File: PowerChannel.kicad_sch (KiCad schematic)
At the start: 15 parts, among them J1 Screw_Terminal_01x04, Q1 2N7002, Q2 NTF6P02, Q3 2N7002, U12 INA219xID

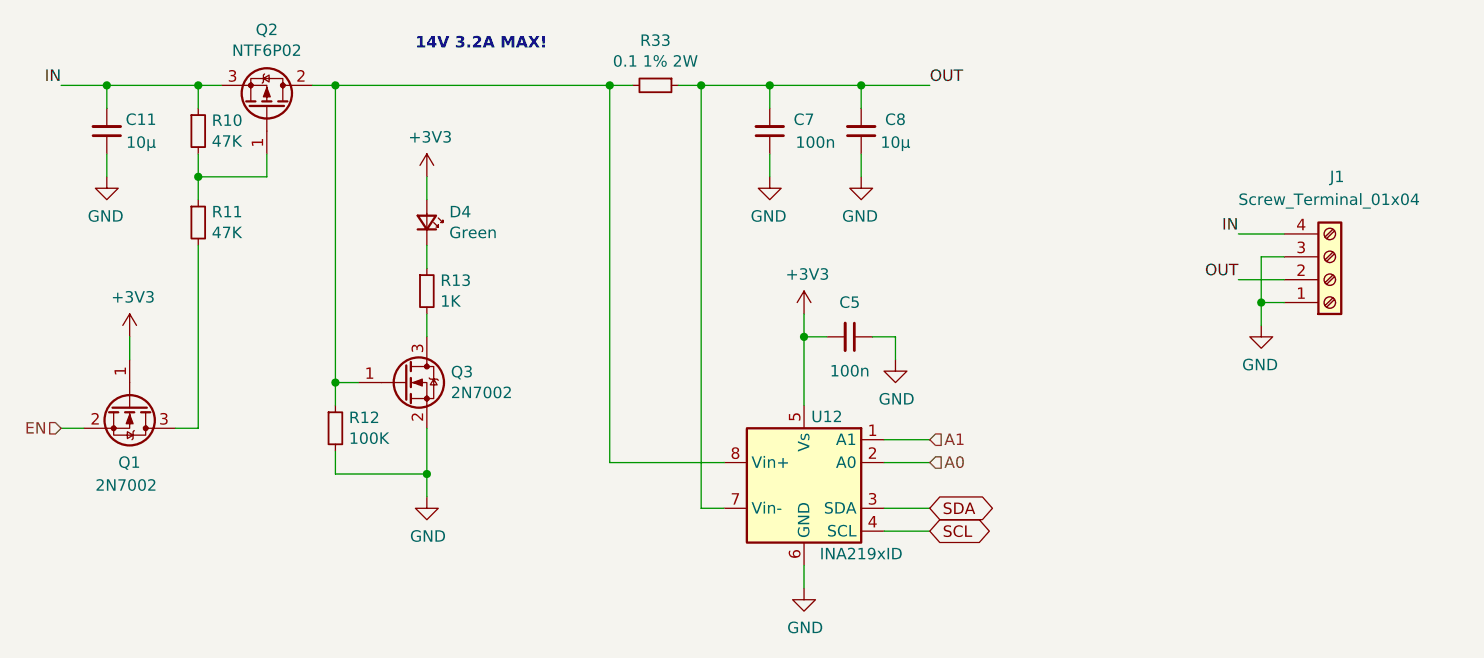
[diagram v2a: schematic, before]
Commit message: Schematic: Replace Teensy 3.2 by PCF8574
Signed-off-by: Geert Uytterhoeven <geert@linux-m68k.org>
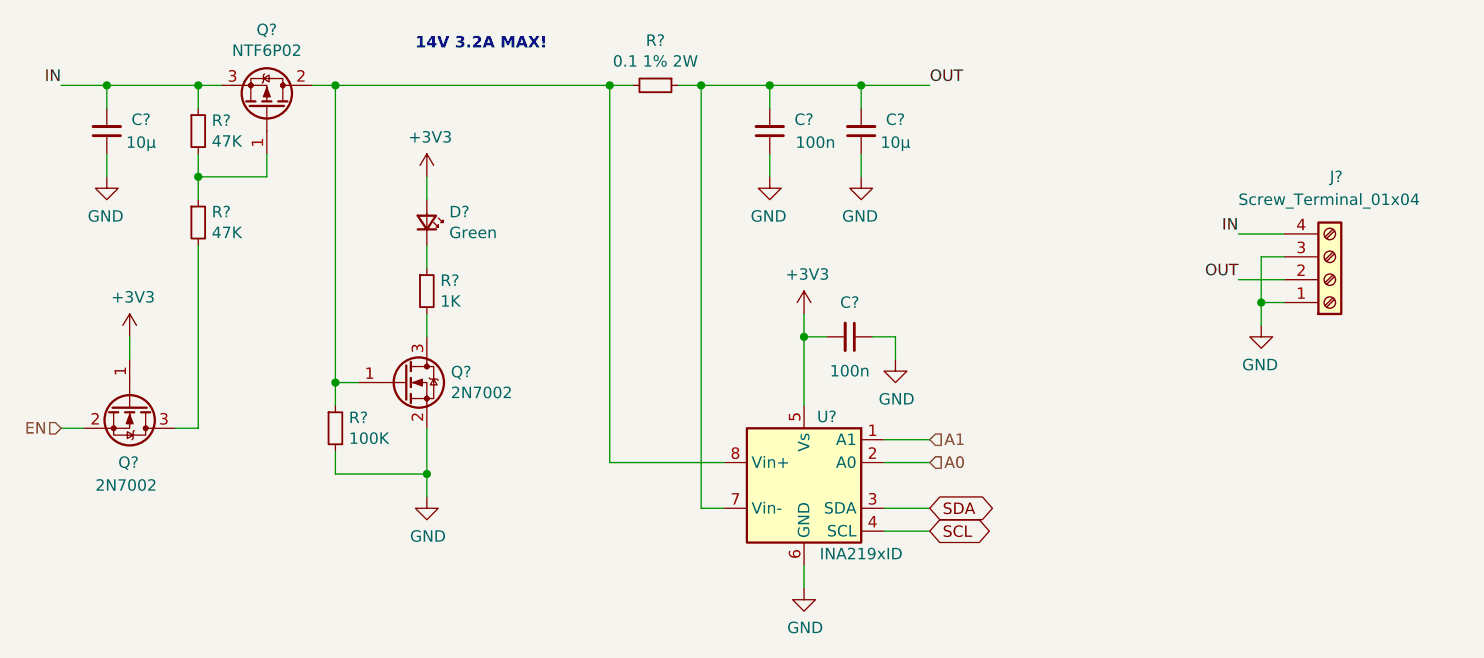
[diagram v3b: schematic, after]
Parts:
- renumbered C5 to C?, C7 to C?, C8 to C?, C11 to C?, D4 to D?, J1 to J?, Q2 to Q?, Q1 to Q?, Q3 to Q?, R11 to R?, R10 to R?, R12 to R?, R13 to R?, R33 to R?, U12 to U?
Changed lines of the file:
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@@
   (symbol (lib_id "Device:R_Small") (at 53.34 40.64 0)
     (in_bom yes) (on_board yes)
-    (property "Reference" "R11" (id 0) (at 54.8386 39.4716 0)
+    (property "Reference" "R?" (id 0) (at 54.8386 39.4716 0)
       (effects (font (size 1.27 1.27)) (justify left))
     )
@@
   (symbol (lib_id "Device:R_Small") (at 53.34 30.48 0)
     (in_bom yes) (on_board yes)
-    (property "Reference" "R10" (id 0) (at 54.8386 29.3116 0)
+    (property "Reference" "R?" (id 0) (at 54.8386 29.3116 0)
       (effects (font (size 1.27 1.27)) (justify left))
     )
@@
   (symbol (lib_id "Transistor_FET:IRF9540N") (at 60.96 27.94 270) (mirror x)
     (in_bom yes) (on_board yes)
-    (property "Reference" "Q2" (id 0) (at 60.96 19.2278 90))
+    (property "Reference" "Q?" (id 0) (at 60.96 19.2278 90))
     (property "Value" "NTF6P02" (id 1) (at 60.96 21.5392 90))
     (property "Footprint" "Package_TO_SOT_SMD:SOT-223-3_TabPin2" (id 2) (at 59.055 22.86 0)
@@
   (symbol (lib_id "Device:R_Small") (at 68.58 63.5 0)
     (in_bom yes) (on_board yes)
-    (property "Reference" "R12" (id 0) (at 70.0786 62.3316 0)
+    (property "Reference" "R?" (id 0) (at 70.0786 62.3316 0)
       (effects (font (size 1.27 1.27)) (justify left))
     )
@@
   (symbol (lib_id "power:GND") (at 78.74 71.12 0)
     (in_bom yes) (on_board yes)
-    (property "Reference" "#PWR08" (id 0) (at 78.74 77.47 0)
+    (property "Reference" "#PWR?" (id 0) (at 78.74 77.47 0)
       (effects (font (size 1.27 1.27)) hide)
     )
@@
   (symbol (lib_id "Device:R_Small") (at 78.74 48.26 0)
     (in_bom yes) (on_board yes)
-    (property "Reference" "R13" (id 0) (at 80.2386 47.0916 0)
+    (property "Reference" "R?" (id 0) (at 80.2386 47.0916 0)
       (effects (font (size 1.27 1.27)) (justify left))
     )
@@
   (symbol (lib_id "power:+3V3") (at 78.74 35.56 0)
     (in_bom yes) (on_board yes)
-    (property "Reference" "#PWR07" (id 0) (at 78.74 39.37 0)
+    (property "Reference" "#PWR?" (id 0) (at 78.74 39.37 0)
       (effects (font (size 1.27 1.27)) hide)
     )
@@
   (symbol (lib_id "Connector:Screw_Terminal_01x04") (at 179.07 46.99 0) (mirror x)
     (in_bom yes) (on_board yes)
-    (property "Reference" "J1" (id 0) (at 179.07 35.56 0)
+    (property "Reference" "J?" (id 0) (at 179.07 35.56 0)
       (effects (font (size 1.27 1.27)) (justify left))
     )
@@
   (symbol (lib_id "power:GND") (at 171.45 52.07 0) (mirror y)
     (in_bom yes) (on_board yes)
-    (property "Reference" "#PWR09" (id 0) (at 171.45 58.42 0)
+    (property "Reference" "#PWR?" (id 0) (at 171.45 58.42 0)
       (effects (font (size 1.27 1.27)) hide)
     )
@@
   (symbol (lib_id "Device:LED_Small") (at 78.74 40.64 270) (mirror x)
     (in_bom yes) (on_board yes)
-    (property "Reference" "D4" (id 0) (at 81.2292 39.4716 90)
+    (property "Reference" "D?" (id 0) (at 81.2292 39.4716 90)
       (effects (font (size 1.27 1.27)) (justify left))
     )
@@
   (symbol (lib_id "Transistor_FET:2N7002") (at 45.72 60.96 270)
     (in_bom yes) (on_board yes)
-    (property "Reference" "Q1" (id 0) (at 44.45 67.31 90)
+    (property "Reference" "Q?" (id 0) (at 44.45 67.31 90)
       (effects (font (size 1.27 1.27)) (justify left))
     )
@@
   (symbol (lib_id "Transistor_FET:2N7002") (at 76.2 58.42 0)
     (in_bom yes) (on_board yes)
-    (property "Reference" "Q3" (id 0) (at 81.407 57.2516 0)
+    (property "Reference" "Q?" (id 0) (at 81.407 57.2516 0)
       (effects (font (size 1.27 1.27)) (justify left))
     )
@@
   (symbol (lib_id "Device:R_Small") (at 104.14 25.4 270)
     (in_bom yes) (on_board yes)
-    (property "Reference" "R33" (id 0) (at 104.14 20.4216 90))
+    (property "Reference" "R?" (id 0) (at 104.14 20.4216 90))
     (property "Value" "0.1 1% 2W" (id 1) (at 104.14 22.733 90))
     (property "Footprint" "Resistor_SMD:R_2512_6332Metric_Pad1.52x3.35mm_HandSolder" (id 2) (at 104.14 25.4 0)
@@
   (symbol (lib_id "power:GND") (at 120.65 81.28 0)
     (in_bom yes) (on_board yes)
-    (property "Reference" "#PWR0108" (id 0) (at 120.65 87.63 0)
+    (property "Reference" "#PWR?" (id 0) (at 120.65 87.63 0)
       (effects (font (size 1.27 1.27)) hide)
     )
@@
   (symbol (lib_id "power:+3V3") (at 120.65 50.8 0)
     (in_bom yes) (on_board yes)
-    (property "Reference" "#PWR0109" (id 0) (at 120.65 54.61 0)
+    (property "Reference" "#PWR?" (id 0) (at 120.65 54.61 0)
       (effects (font (size 1.27 1.27)) hide)
     )
@@
   (symbol (lib_id "Device:C_Small") (at 125.73 53.34 270)
     (in_bom yes) (on_board yes)
-    (property "Reference" "C5" (id 0) (at 125.73 49.53 90))
+    (property "Reference" "C?" (id 0) (at 125.73 49.53 90))
     (property "Value" "100n" (id 1) (at 125.73 57.15 90))
     (property "Footprint" "Capacitor_SMD:C_0603_1608Metric_Pad1.05x0.95mm_HandSolder" (id 2) (at 125.73 53.34 0)
@@
   (symbol (lib_id "Device:C_Small") (at 116.84 30.48 180)
     (in_bom yes) (on_board yes)
-    (property "Reference" "C7" (id 0) (at 120.65 29.21 0))
+    (property "Reference" "C?" (id 0) (at 120.65 29.21 0))
     (property "Value" "100n" (id 1) (at 121.92 31.75 0))
     (property "Footprint" "Capacitor_SMD:C_0603_1608Metric_Pad1.05x0.95mm_HandSolder" (id 2) (at 116.84 30.48 0)
@@
   (symbol (lib_id "Device:C_Small") (at 127 30.48 180)
     (in_bom yes) (on_board yes)
-    (property "Reference" "C8" (id 0) (at 130.81 29.21 0))
+    (property "Reference" "C?" (id 0) (at 130.81 29.21 0))
     (property "Value" "10µ" (id 1) (at 130.81 31.75 0))
     (property "Footprint" "Capacitor_SMD:C_0805_2012Metric_Pad1.15x1.40mm_HandSolder" (id 2) (at 127 30.48 0)
@@
   (symbol (lib_id "power:GND") (at 116.84 35.56 0) (mirror y)
     (in_bom yes) (on_board yes)
-    (property "Reference" "#PWR025" (id 0) (at 116.84 41.91 0)
+    (property "Reference" "#PWR?" (id 0) (at 116.84 41.91 0)
       (effects (font (size 1.27 1.27)) hide)
     )
@@
   (symbol (lib_id "power:GND") (at 127 35.56 0) (mirror y)
     (in_bom yes) (on_board yes)
-    (property "Reference" "#PWR030" (id 0) (at 127 41.91 0)
+    (property "Reference" "#PWR?" (id 0) (at 127 41.91 0)
       (effects (font (size 1.27 1.27)) hide)
     )
@@
   (symbol (lib_id "Device:C_Small") (at 43.18 30.48 180)
     (in_bom yes) (on_board yes)
-    (property "Reference" "C11" (id 0) (at 46.99 29.21 0))
+    (property "Reference" "C?" (id 0) (at 46.99 29.21 0))
     (property "Value" "10µ" (id 1) (at 46.99 31.75 0))
     (property "Footprint" "Capacitor_SMD:C_0805_2012Metric_Pad1.15x1.40mm_HandSolder" (id 2) (at 43.18 30.48 0)
@@
   (symbol (lib_id "power:GND") (at 43.18 35.56 0) (mirror y)
     (in_bom yes) (on_board yes)
-    (property "Reference" "#PWR033" (id 0) (at 43.18 41.91 0)
+    (property "Reference" "#PWR?" (id 0) (at 43.18 41.91 0)
       (effects (font (size 1.27 1.27)) hide)
     )
@@
   (symbol (lib_id "INA219:INA219xID") (at 120.65 69.85 0)
     (in_bom yes) (on_board yes)
-    (property "Reference" "U12" (id 0) (at 123.19 62.23 0))
+    (property "Reference" "U?" (id 0) (at 123.19 62.23 0))
     (property "Value" "INA219xID" (id 1) (at 127 77.47 0))
     (property "Footprint" "Package_SO:SOIC-8_3.9x4.9mm_P1.27mm" (id 2) (at 129.54 69.85 0)
@@
   (symbol (lib_id "power:GND") (at 130.81 55.88 0)
     (in_bom yes) (on_board yes)
-    (property "Reference" "#PWR043" (id 0) (at 130.81 62.23 0)
-      (effects (font (size 1.27 1.27)) hide)
-    )
+    (property "Reference" "#PWR?" (id 0) (at 130.81 62.23 0)
+      (effects (font (size 1.27 1.27)) hide)
+    )

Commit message: Schematic: Annotate symbol references
Fill in schematic symbol reference designators.

Signed-off-by: Geert Uytterhoeven <geert@linux-m68k.org>
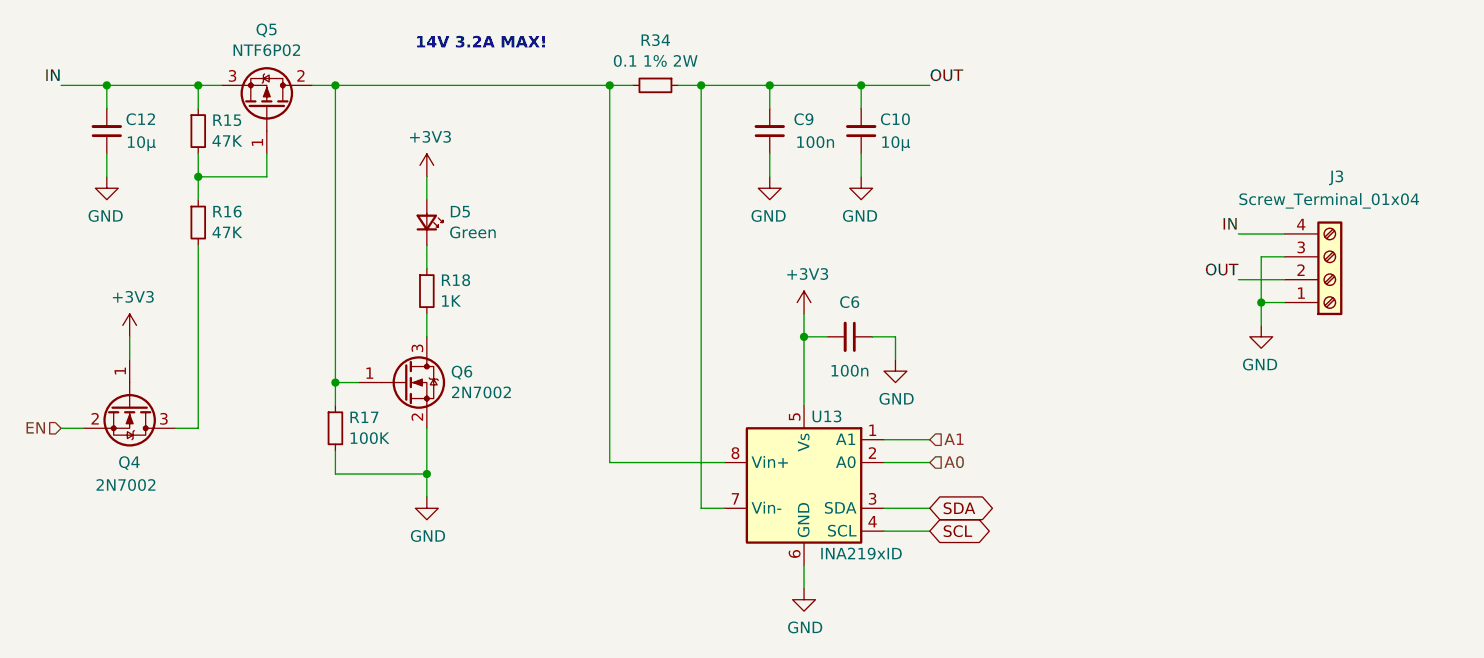
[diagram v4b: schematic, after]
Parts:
- gave numbers to parts that had none: 15
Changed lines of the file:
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@@
   (symbol (lib_id "Device:R_Small") (at 53.34 40.64 0)
     (in_bom yes) (on_board yes)
-    (property "Reference" "R?" (id 0) (at 54.8386 39.4716 0)
+    (property "Reference" "R16" (id 0) (at 54.8386 39.4716 0)
       (effects (font (size 1.27 1.27)) (justify left))
     )
@@
   (symbol (lib_id "Device:R_Small") (at 53.34 30.48 0)
     (in_bom yes) (on_board yes)
-    (property "Reference" "R?" (id 0) (at 54.8386 29.3116 0)
+    (property "Reference" "R15" (id 0) (at 54.8386 29.3116 0)
       (effects (font (size 1.27 1.27)) (justify left))
     )
@@
   (symbol (lib_id "Transistor_FET:IRF9540N") (at 60.96 27.94 270) (mirror x)
     (in_bom yes) (on_board yes)
-    (property "Reference" "Q?" (id 0) (at 60.96 19.2278 90))
+    (property "Reference" "Q5" (id 0) (at 60.96 19.2278 90))
     (property "Value" "NTF6P02" (id 1) (at 60.96 21.5392 90))
     (property "Footprint" "Package_TO_SOT_SMD:SOT-223-3_TabPin2" (id 2) (at 59.055 22.86 0)
@@
   (symbol (lib_id "Device:R_Small") (at 68.58 63.5 0)
     (in_bom yes) (on_board yes)
-    (property "Reference" "R?" (id 0) (at 70.0786 62.3316 0)
+    (property "Reference" "R17" (id 0) (at 70.0786 62.3316 0)
       (effects (font (size 1.27 1.27)) (justify left))
     )
@@
   (symbol (lib_id "power:GND") (at 78.74 71.12 0)
     (in_bom yes) (on_board yes)
-    (property "Reference" "#PWR?" (id 0) (at 78.74 77.47 0)
+    (property "Reference" "#PWR012" (id 0) (at 78.74 77.47 0)
       (effects (font (size 1.27 1.27)) hide)
     )
@@
   (symbol (lib_id "Device:R_Small") (at 78.74 48.26 0)
     (in_bom yes) (on_board yes)
-    (property "Reference" "R?" (id 0) (at 80.2386 47.0916 0)
+    (property "Reference" "R18" (id 0) (at 80.2386 47.0916 0)
       (effects (font (size 1.27 1.27)) (justify left))
     )
@@
   (symbol (lib_id "power:+3V3") (at 78.74 35.56 0)
     (in_bom yes) (on_board yes)
-    (property "Reference" "#PWR?" (id 0) (at 78.74 39.37 0)
+    (property "Reference" "#PWR011" (id 0) (at 78.74 39.37 0)
       (effects (font (size 1.27 1.27)) hide)
     )
@@
   (symbol (lib_id "Connector:Screw_Terminal_01x04") (at 179.07 46.99 0) (mirror x)
     (in_bom yes) (on_board yes)
-    (property "Reference" "J?" (id 0) (at 179.07 35.56 0)
+    (property "Reference" "J3" (id 0) (at 179.07 35.56 0)
       (effects (font (size 1.27 1.27)) (justify left))
     )
@@
   (symbol (lib_id "power:GND") (at 171.45 52.07 0) (mirror y)
     (in_bom yes) (on_board yes)
-    (property "Reference" "#PWR?" (id 0) (at 171.45 58.42 0)
+    (property "Reference" "#PWR013" (id 0) (at 171.45 58.42 0)
       (effects (font (size 1.27 1.27)) hide)
     )
@@
   (symbol (lib_id "Device:LED_Small") (at 78.74 40.64 270) (mirror x)
     (in_bom yes) (on_board yes)
-    (property "Reference" "D?" (id 0) (at 81.2292 39.4716 90)
+    (property "Reference" "D5" (id 0) (at 81.2292 39.4716 90)
       (effects (font (size 1.27 1.27)) (justify left))
     )
@@
   (symbol (lib_id "Transistor_FET:2N7002") (at 45.72 60.96 270)
     (in_bom yes) (on_board yes)
-    (property "Reference" "Q?" (id 0) (at 44.45 67.31 90)
+    (property "Reference" "Q4" (id 0) (at 44.45 67.31 90)
       (effects (font (size 1.27 1.27)) (justify left))
     )
@@
   (symbol (lib_id "Transistor_FET:2N7002") (at 76.2 58.42 0)
     (in_bom yes) (on_board yes)
-    (property "Reference" "Q?" (id 0) (at 81.407 57.2516 0)
+    (property "Reference" "Q6" (id 0) (at 81.407 57.2516 0)
       (effects (font (size 1.27 1.27)) (justify left))
     )
@@
   (symbol (lib_id "Device:R_Small") (at 104.14 25.4 270)
     (in_bom yes) (on_board yes)
-    (property "Reference" "R?" (id 0) (at 104.14 20.4216 90))
+    (property "Reference" "R34" (id 0) (at 104.14 20.4216 90))
     (property "Value" "0.1 1% 2W" (id 1) (at 104.14 22.733 90))
     (property "Footprint" "Resistor_SMD:R_2512_6332Metric_Pad1.52x3.35mm_HandSolder" (id 2) (at 104.14 25.4 0)
@@
   (symbol (lib_id "power:GND") (at 120.65 81.28 0)
     (in_bom yes) (on_board yes)
-    (property "Reference" "#PWR?" (id 0) (at 120.65 87.63 0)
+    (property "Reference" "#PWR0110" (id 0) (at 120.65 87.63 0)
       (effects (font (size 1.27 1.27)) hide)
     )
@@
   (symbol (lib_id "power:+3V3") (at 120.65 50.8 0)
     (in_bom yes) (on_board yes)
-    (property "Reference" "#PWR?" (id 0) (at 120.65 54.61 0)
+    (property "Reference" "#PWR0111" (id 0) (at 120.65 54.61 0)
       (effects (font (size 1.27 1.27)) hide)
     )
@@
   (symbol (lib_id "Device:C_Small") (at 125.73 53.34 270)
     (in_bom yes) (on_board yes)
-    (property "Reference" "C?" (id 0) (at 125.73 49.53 90))
+    (property "Reference" "C6" (id 0) (at 125.73 49.53 90))
     (property "Value" "100n" (id 1) (at 125.73 57.15 90))
     (property "Footprint" "Capacitor_SMD:C_0603_1608Metric_Pad1.05x0.95mm_HandSolder" (id 2) (at 125.73 53.34 0)
@@
   (symbol (lib_id "Device:C_Small") (at 116.84 30.48 180)
     (in_bom yes) (on_board yes)
-    (property "Reference" "C?" (id 0) (at 120.65 29.21 0))
+    (property "Reference" "C9" (id 0) (at 120.65 29.21 0))
     (property "Value" "100n" (id 1) (at 121.92 31.75 0))
     (property "Footprint" "Capacitor_SMD:C_0603_1608Metric_Pad1.05x0.95mm_HandSolder" (id 2) (at 116.84 30.48 0)
@@
   (symbol (lib_id "Device:C_Small") (at 127 30.48 180)
     (in_bom yes) (on_board yes)
-    (property "Reference" "C?" (id 0) (at 130.81 29.21 0))
+    (property "Reference" "C10" (id 0) (at 130.81 29.21 0))
     (property "Value" "10µ" (id 1) (at 130.81 31.75 0))
     (property "Footprint" "Capacitor_SMD:C_0805_2012Metric_Pad1.15x1.40mm_HandSolder" (id 2) (at 127 30.48 0)
@@
   (symbol (lib_id "power:GND") (at 116.84 35.56 0) (mirror y)
     (in_bom yes) (on_board yes)
-    (property "Reference" "#PWR?" (id 0) (at 116.84 41.91 0)
+    (property "Reference" "#PWR031" (id 0) (at 116.84 41.91 0)
       (effects (font (size 1.27 1.27)) hide)
     )
@@
   (symbol (lib_id "power:GND") (at 127 35.56 0) (mirror y)
     (in_bom yes) (on_board yes)
-    (property "Reference" "#PWR?" (id 0) (at 127 41.91 0)
+    (property "Reference" "#PWR032" (id 0) (at 127 41.91 0)
       (effects (font (size 1.27 1.27)) hide)
     )
@@
   (symbol (lib_id "Device:C_Small") (at 43.18 30.48 180)
     (in_bom yes) (on_board yes)
-    (property "Reference" "C?" (id 0) (at 46.99 29.21 0))
+    (property "Reference" "C12" (id 0) (at 46.99 29.21 0))
     (property "Value" "10µ" (id 1) (at 46.99 31.75 0))
     (property "Footprint" "Capacitor_SMD:C_0805_2012Metric_Pad1.15x1.40mm_HandSolder" (id 2) (at 43.18 30.48 0)
@@
   (symbol (lib_id "power:GND") (at 43.18 35.56 0) (mirror y)
     (in_bom yes) (on_board yes)
-    (property "Reference" "#PWR?" (id 0) (at 43.18 41.91 0)
+    (property "Reference" "#PWR034" (id 0) (at 43.18 41.91 0)
       (effects (font (size 1.27 1.27)) hide)
     )
@@
   (symbol (lib_id "INA219:INA219xID") (at 120.65 69.85 0)
     (in_bom yes) (on_board yes)
-    (property "Reference" "U?" (id 0) (at 123.19 62.23 0))
+    (property "Reference" "U13" (id 0) (at 123.19 62.23 0))
     (property "Value" "INA219xID" (id 1) (at 127 77.47 0))
     (property "Footprint" "Package_SO:SOIC-8_3.9x4.9mm_P1.27mm" (id 2) (at 129.54 69.85 0)
@@
   (symbol (lib_id "power:GND") (at 130.81 55.88 0)
     (in_bom yes) (on_board yes)
-    (property "Reference" "#PWR?" (id 0) (at 130.81 62.23 0)
+    (property "Reference" "#PWR044" (id 0) (at 130.81 62.23 0)
       (effects (font (size 1.27 1.27)) hide)
     )
@@
   (symbol (lib_id "power:+3V3") (at 45.72 53.34 0)
     (in_bom yes) (on_board yes)
-    (property "Reference" "#PWR?" (id 0) (at 45.72 57.15 0)
-      (effects (font (size 1.27 1.27)) hide)
-    )
+    (property "Reference" "#PWR020" (id 0) (at 45.72 57.15 0)
+      (effects (font (size 1.27 1.27)) hide)
+    )
